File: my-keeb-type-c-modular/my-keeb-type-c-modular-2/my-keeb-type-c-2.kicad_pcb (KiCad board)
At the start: 2 copper layers, 190.5 x 99.8 mm, 115 parts, among them J1 AVR-ISP-6, SW1 SW_Push, U1 ATmega32U4-AU, U2 PRTR5V0U2X, Y1 16MHz

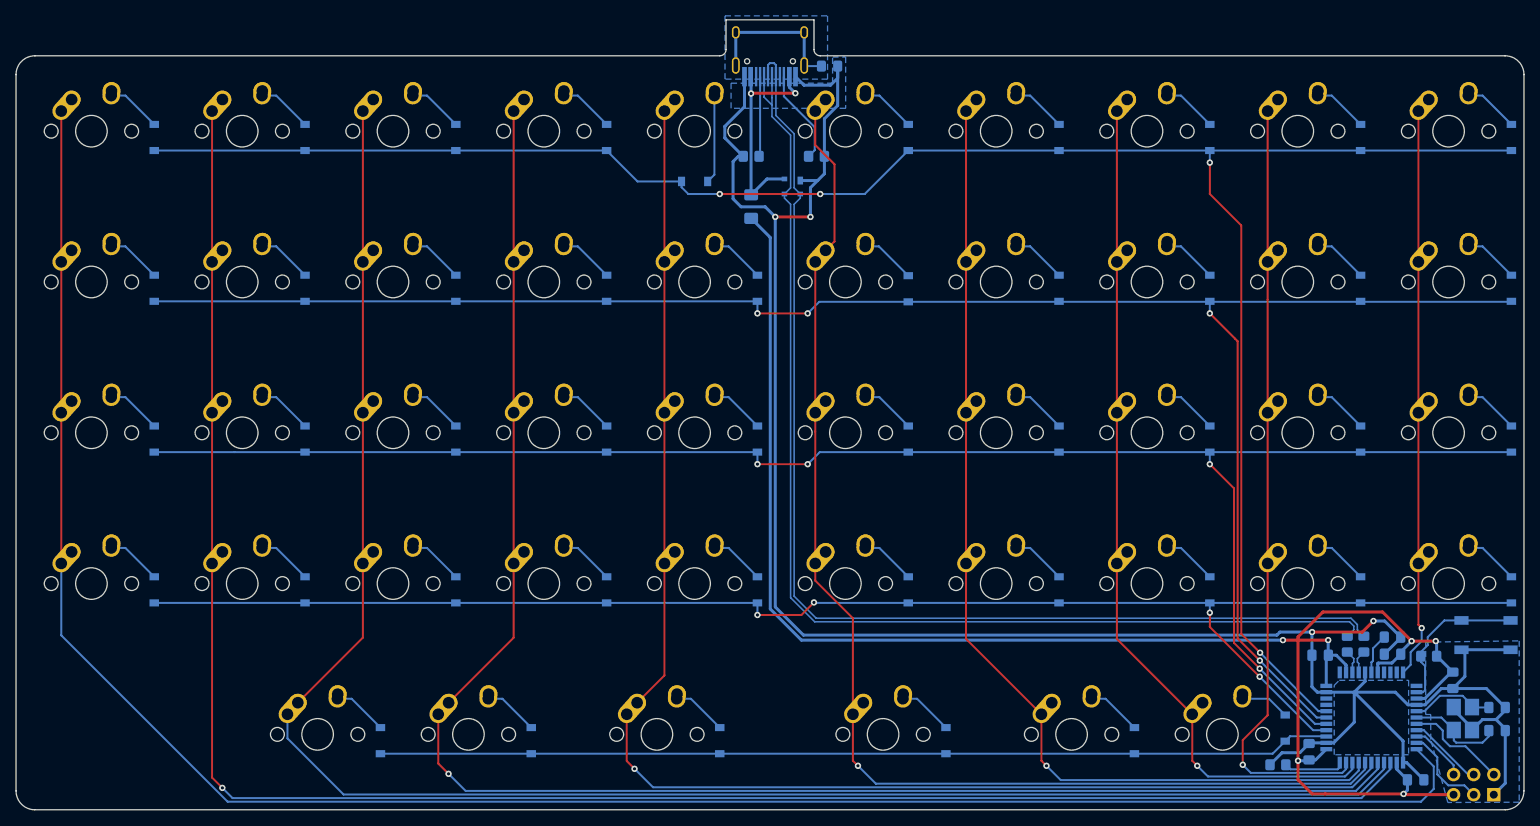
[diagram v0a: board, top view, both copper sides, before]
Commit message: Finished type c part 2 and updated type c part 1
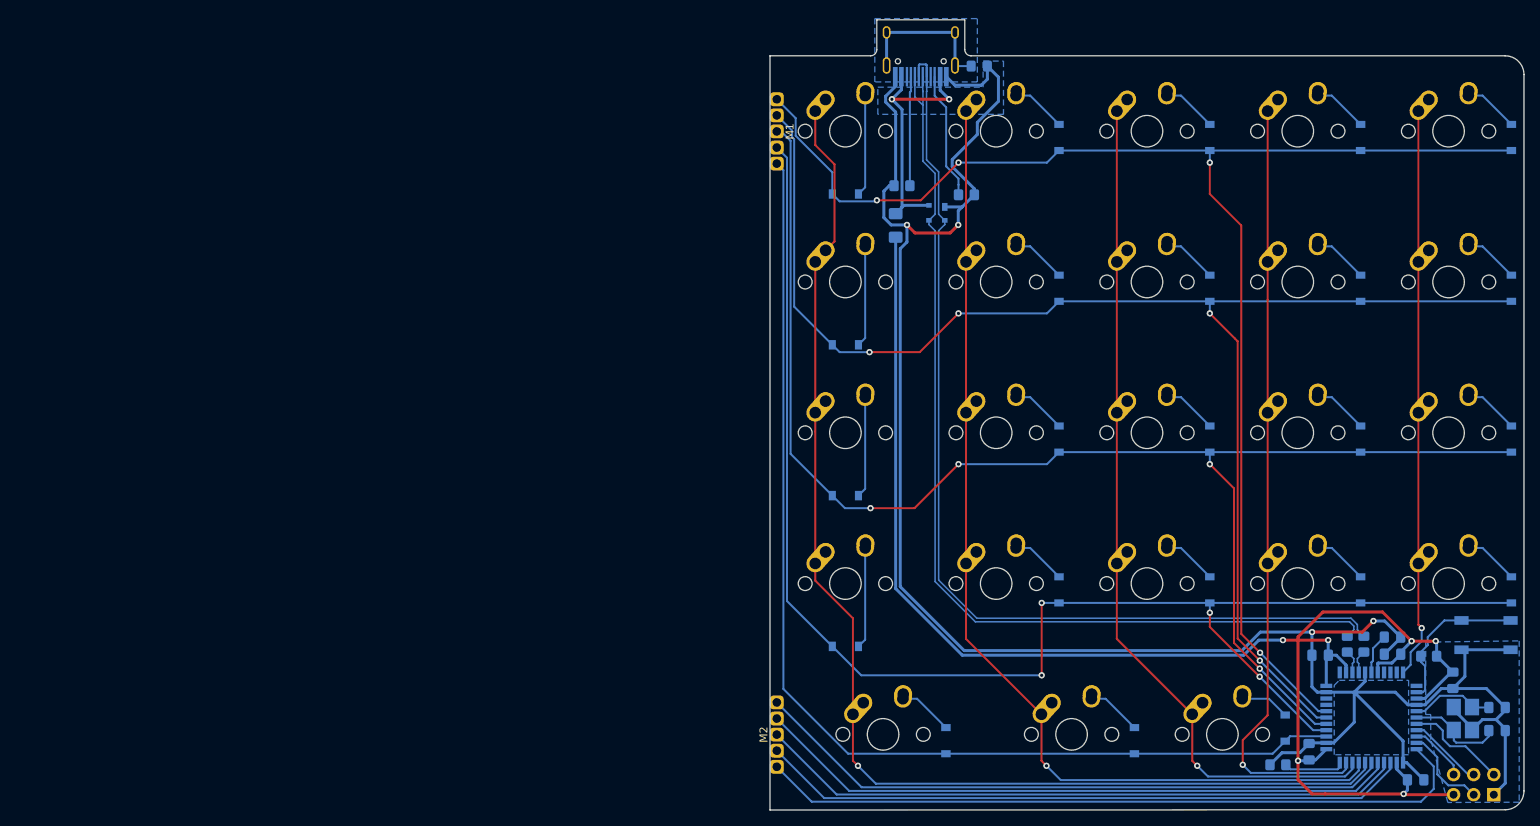
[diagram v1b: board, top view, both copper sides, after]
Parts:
- removed D1, D10, D11, D12, D13, D14, D15, D16, D17, D18, D19, D2, D20, D21, D22, D23, D3, D4, D5, D6, D7, D8, D9: SOD-123, Diode_SMD:D_SOD-123
- removed G***: LOGO, sasha:B.SilkS_layer1
- removed MX1, MX10, MX11, MX12, MX13, MX14, MX15, MX16, MX17, MX18, MX19, MX2, MX20, MX21, MX22, MX3, MX4, MX5, MX6, MX7, MX8, MX9: MX-NoLED, MX_Alps_Hybrid:MX-1U-NoLED
- removed MX23: MX-NoLED, MX_Alps_Hybrid:MX-1.5U-NoLED
- added M1: 1x5, modular:1x5, F.Cu at (117.5, 30.5)
- added M2: 1x5, modular:1x5, F.Cu at (117.5, 107.7)
- moved R3 19.6 mm to (141.5, 39.0)
- moved R4 19.4 mm to (133.3, 37.8)
- moved USB1 19.0 mm to (135.7, 15.9)
- moved FB1 18.9 mm to (143.1, 22.7)
- moved U2 18.6 mm to (137.8, 41.3)
- moved F1 18.4 mm to (132.6, 42.9)
- moved D26 10.7 mm to (126.2, 77.0), turned to 0 degrees
- moved D24 10.7 mm to (126.2, 38.9), turned to 0 degrees
- moved D27 10.7 mm to (126.2, 96.0), turned to 0 degrees
- moved D25 10.6 mm to (126.2, 57.9), turned to 0 degrees
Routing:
- net COL0: track 254.9 -> 91.4 mm
- net COL1: track 236.5 -> 82.3 mm, vias 1 -> 0
- net COL2: track 224.8 -> 82.0 mm
- net COL3: track 206.4 -> 81.7 mm, vias 1 -> 0
- net COL4: track 179.2 -> 81.2 mm, vias 1 -> 0
- net ROW0: track 253.9 -> 181.2 mm
- net ROW1: track 233.0 -> 180.2 mm
- net ROW2: track 214.9 -> 179.9 mm
- net DP: track 145.8 -> 125.9 mm
- net DN: track 145.7 -> 125.9 mm
- net ROW4: track 120.4 -> 139.6 mm
- net +5V: track 217.3 -> 198.2 mm
- net ROW3: track 196.8 -> 185.5 mm
- net Net-(D19-Pad2): track 11.2 -> 0.00 mm
- net GND: track 294.6 -> 284.1 mm
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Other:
- board size 190.5 x 99.8 mm -> 95.3 x 99.8 mm
- board text removed: "salsa"
